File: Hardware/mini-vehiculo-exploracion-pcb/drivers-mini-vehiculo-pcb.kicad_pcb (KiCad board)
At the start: 2 copper layers, 26 parts, among them IC1 MAX8891EXK33_V+T, J1 Conn_01x08_Pin_drv, U1 DRV8873HPWPRQ1, U2 DRV8873HPWPRQ1, U3 TPS561208DDCR

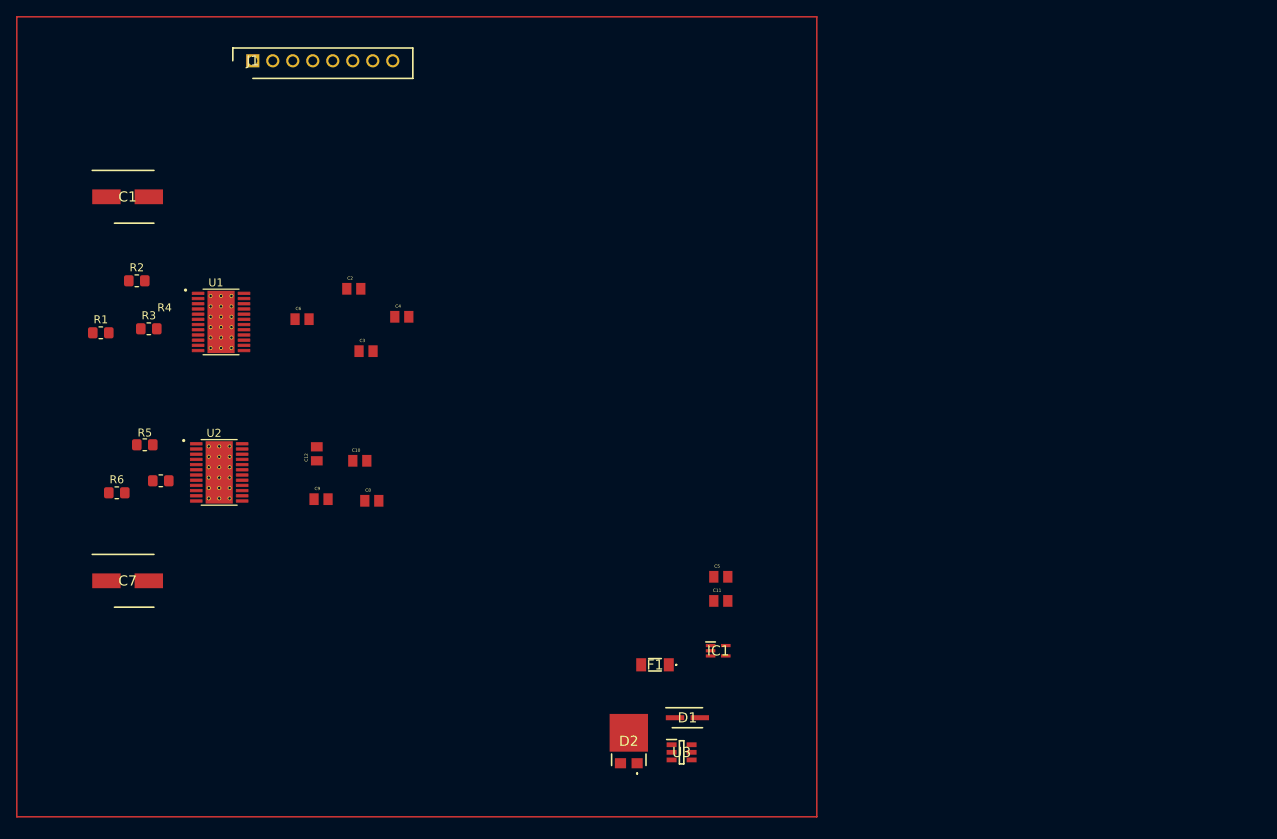
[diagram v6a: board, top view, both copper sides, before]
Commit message: adicion de bornera pcb drivers y organizacion de entrada
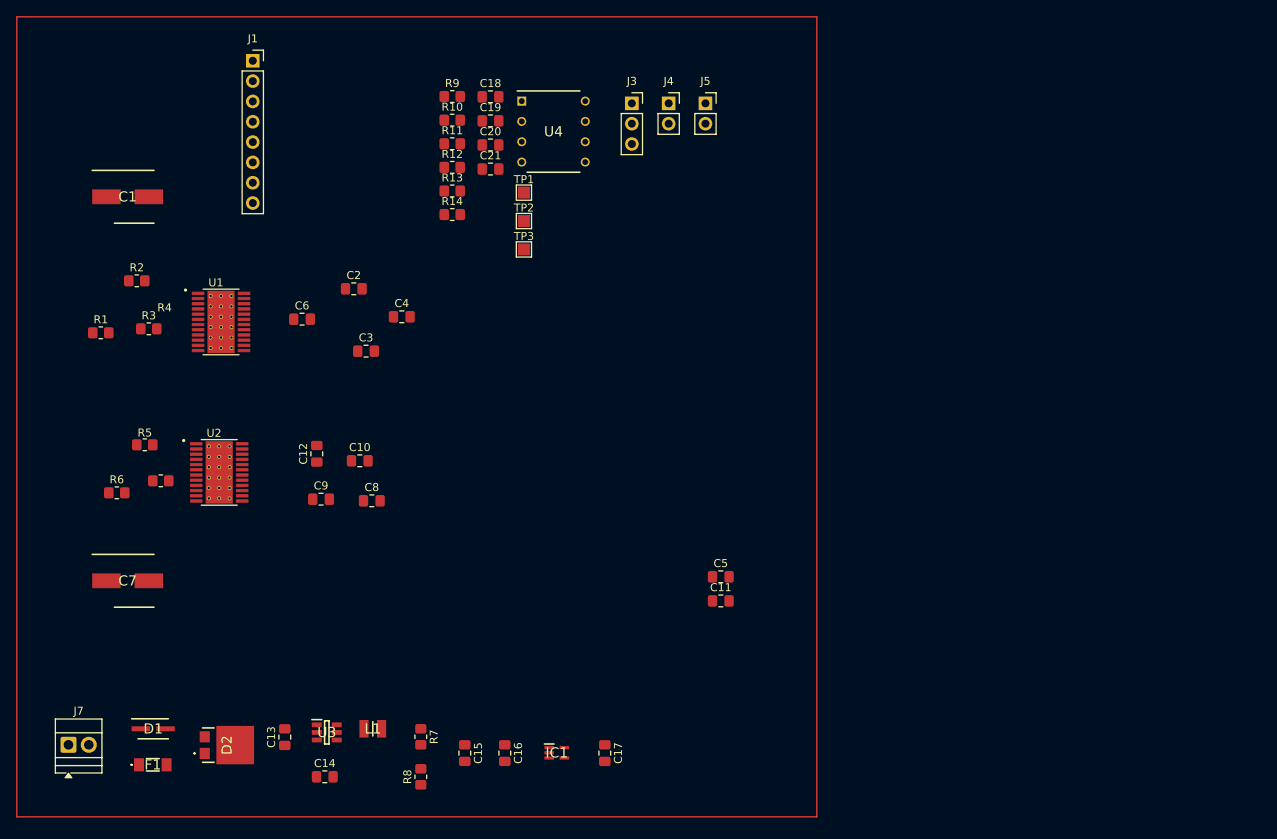
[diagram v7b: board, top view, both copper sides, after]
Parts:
- added C13: 10u, Capacitor_SMD:C_0805_2012Metric_Pad1.18x1.45mm_HandSolder, F.Cu at (58.0, 129.0)
- added C14: 100n, Capacitor_SMD:C_0805_2012Metric_Pad1.18x1.45mm_HandSolder, F.Cu at (63.0, 134.0)
- added C15: 47u, Capacitor_SMD:C_0805_2012Metric_Pad1.18x1.45mm_HandSolder, F.Cu at (80.5, 131.0)
- added C16: 1u, Capacitor_SMD:C_0805_2012Metric_Pad1.18x1.45mm_HandSolder, F.Cu at (85.5, 131.0)
- added C17: 1u, Capacitor_SMD:C_0805_2012Metric_Pad1.18x1.45mm_HandSolder, F.Cu at (98.0, 131.0)
- added C18: 10uF, Capacitor_SMD:C_0805_2012Metric_Pad1.18x1.45mm_HandSolder, F.Cu at (83.7, 49.0)
- added C19: 200nF, Capacitor_SMD:C_0805_2012Metric_Pad1.18x1.45mm_HandSolder, F.Cu at (83.7, 52.0)
- added C20: 10uF, Capacitor_SMD:C_0805_2012Metric_Pad1.18x1.45mm_HandSolder, F.Cu at (83.7, 55.0)
- added C21: 4.7u, Capacitor_SMD:C_0805_2012Metric_Pad1.18x1.45mm_HandSolder, F.Cu at (83.7, 58.0)
- added J3: Conn_01x03_Pin, Connector_PinSocket_2.54mm:PinSocket_1x03_P2.54mm_Vertical, F.Cu at (101.4, 49.8)
- added J4: Conn_01x02_Motor1, Connector_PinSocket_2.54mm:PinSocket_1x02_P2.54mm_Vertical, F.Cu at (106.0, 49.8)
- added J5: Conn_01x02_Motor2, Connector_PinSocket_2.54mm:PinSocket_1x02_P2.54mm_Vertical, F.Cu at (110.6, 49.8)
- added J7: Battery_Terminal_01x02, TerminalBlock:TerminalBlock_Xinya_XY308-2.54-2P_1x02_P2.54mm_Horizontal, F.Cu at (31.0, 130.0)
- added L1: MLP2520S4R7MT0S1, MLP2520S4R7MT0S1:INDC2520X100N, F.Cu at (69.0, 128.0)
- added R10: 10k, Resistor_SMD:R_0805_2012Metric_Pad1.20x1.40mm_HandSolder, F.Cu at (78.9, 51.9)
- added R11: 18k, Resistor_SMD:R_0805_2012Metric_Pad1.20x1.40mm_HandSolder, F.Cu at (78.9, 54.9)
- added R12: 20k, Resistor_SMD:R_0805_2012Metric_Pad1.20x1.40mm_HandSolder, F.Cu at (78.9, 57.8)
- added R13: 2k, Resistor_SMD:R_0805_2012Metric_Pad1.20x1.40mm_HandSolder, F.Cu at (78.9, 60.8)
- added R14: 2.7k, Resistor_SMD:R_0805_2012Metric_Pad1.20x1.40mm_HandSolder, F.Cu at (78.9, 63.7)
- added R7: 56,2k, Resistor_SMD:R_0805_2012Metric_Pad1.20x1.40mm_HandSolder, F.Cu at (75.0, 129.0)
- added R8: 10k, Resistor_SMD:R_0805_2012Metric_Pad1.20x1.40mm_HandSolder, F.Cu at (75.0, 134.0)
- added R9: 65k, Resistor_SMD:R_0805_2012Metric_Pad1.20x1.40mm_HandSolder, F.Cu at (78.9, 49.0)
- added TP1: Bat_div, TestPoint:TestPoint_Pad_1.5x1.5mm, F.Cu at (87.9, 61.0)
- added TP2: OP1_Out, TestPoint:TestPoint_Pad_1.5x1.5mm, F.Cu at (87.9, 64.5)
- added TP3: OP2_Out, TestPoint:TestPoint_Pad_1.5x1.5mm, F.Cu at (87.9, 68.1)
- added U4: LM358, LM358AN_NOPB:DIP794W53P254L959H508Q8N, F.Cu at (91.6, 53.4)
- C10, C11, C2, C3, C4, C5, C8, C9: footprint capacitores_driver:CAPC2012X88N -> Capacitor_SMD:C_0805_2012Metric_Pad1.18x1.45mm_HandSolder
- C12, C6: footprint capacitores_driver:CAPC2012X140N -> Capacitor_SMD:C_0805_2012Metric_Pad1.18x1.45mm_HandSolder
- J1: footprint JST_Connectors:JST_8PIN -> Connector_PinSocket_2.54mm:PinSocket_1x08_P2.54mm_Vertical
- U1, U2: footprint DRV8873HPWPRQ1:DRV8873HPWPRQ1 -> DRV8873HPWPRQ1:SOP65P640X120-25N
- moved D1 66.8 mm to (41.5, 128.0)
- moved F1 64.0 mm to (41.5, 132.5), turned to 0 degrees
- moved D2 50.2 mm to (50.8, 130.0), turned to -90 degrees
- moved U3 44.4 mm to (63.2, 128.4)
- moved IC1 23.9 mm to (92.0, 131.0)
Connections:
- C11 pad 1: DVDD -> DVDD_2
- C5 pad 1: DVDD -> DVDD_1
- IC1 pad 2: Net-(IC1-GND) -> GND
- U1 pad 1: DVDD -> DVDD_1
- U1 pad 11: DVDD -> DVDD_1
- U1 pad 25: Net-(U1-EXP-Pad25) -> unconnected-(U1-EXP-Pad25)_18
- U1 pad 3: DVDD -> DVDD_1
- U1 pad P1: Net-(U1-EXP-Pad25) -> unconnected-(U1-EXP-Pad25)_5
- U1 pad P10: Net-(U1-EXP-Pad25) -> unconnected-(U1-EXP-Pad25)_15
- U1 pad P11: Net-(U1-EXP-Pad25) -> unconnected-(U1-EXP-Pad25)_8
- U1 pad P12: Net-(U1-EXP-Pad25) -> unconnected-(U1-EXP-Pad25)_4
- U1 pad P13: Net-(U1-EXP-Pad25) -> unconnected-(U1-EXP-Pad25)_9
- U1 pad P14: Net-(U1-EXP-Pad25) -> unconnected-(U1-EXP-Pad25)_16
- U1 pad P15: Net-(U1-EXP-Pad25) -> unconnected-(U1-EXP-Pad25)_6
- U1 pad P16: Net-(U1-EXP-Pad25) -> unconnected-(U1-EXP-Pad25)_10
- U1 pad P17: Net-(U1-EXP-Pad25) -> unconnected-(U1-EXP-Pad25)
- U1 pad P18: Net-(U1-EXP-Pad25) -> unconnected-(U1-EXP-Pad25)_11
- U1 pad P2: Net-(U1-EXP-Pad25) -> unconnected-(U1-EXP-Pad25)_1
- U1 pad P3: Net-(U1-EXP-Pad25) -> unconnected-(U1-EXP-Pad25)_14
- U1 pad P4: Net-(U1-EXP-Pad25) -> unconnected-(U1-EXP-Pad25)_7
- U1 pad P5: Net-(U1-EXP-Pad25) -> unconnected-(U1-EXP-Pad25)_2
- U1 pad P6: Net-(U1-EXP-Pad25) -> unconnected-(U1-EXP-Pad25)_3
- U1 pad P7: Net-(U1-EXP-Pad25) -> unconnected-(U1-EXP-Pad25)_13
- U1 pad P8: Net-(U1-EXP-Pad25) -> unconnected-(U1-EXP-Pad25)_17
- U1 pad P9: Net-(U1-EXP-Pad25) -> unconnected-(U1-EXP-Pad25)_12
- U2 pad 1: DVDD -> DVDD_2
- U2 pad 11: DVDD -> DVDD_2
- U2 pad 25: Net-(U2-EXP-Pad25) -> unconnected-(U2-EXP-Pad25)_7
- U2 pad 3: DVDD -> DVDD_2
- U2 pad P1: Net-(U2-EXP-Pad25) -> unconnected-(U2-EXP-Pad25)_12
- U2 pad P10: Net-(U2-EXP-Pad25) -> unconnected-(U2-EXP-Pad25)_11
- U2 pad P11: Net-(U2-EXP-Pad25) -> unconnected-(U2-EXP-Pad25)_8
- U2 pad P12: Net-(U2-EXP-Pad25) -> unconnected-(U2-EXP-Pad25)_1
- U2 pad P13: Net-(U2-EXP-Pad25) -> unconnected-(U2-EXP-Pad25)_15
- U2 pad P14: Net-(U2-EXP-Pad25) -> unconnected-(U2-EXP-Pad25)_3
- U2 pad P15: Net-(U2-EXP-Pad25) -> unconnected-(U2-EXP-Pad25)_14
- U2 pad P16: Net-(U2-EXP-Pad25) -> unconnected-(U2-EXP-Pad25)_17
- U2 pad P17: Net-(U2-EXP-Pad25) -> unconnected-(U2-EXP-Pad25)_13
- U2 pad P18: Net-(U2-EXP-Pad25) -> unconnected-(U2-EXP-Pad25)_6
- U2 pad P2: Net-(U2-EXP-Pad25) -> unconnected-(U2-EXP-Pad25)_2
- U2 pad P3: Net-(U2-EXP-Pad25) -> unconnected-(U2-EXP-Pad25)
- U2 pad P4: Net-(U2-EXP-Pad25) -> unconnected-(U2-EXP-Pad25)_18
- U2 pad P5: Net-(U2-EXP-Pad25) -> unconnected-(U2-EXP-Pad25)_5
- U2 pad P6: Net-(U2-EXP-Pad25) -> unconnected-(U2-EXP-Pad25)_16
- U2 pad P7: Net-(U2-EXP-Pad25) -> unconnected-(U2-EXP-Pad25)_10
- U2 pad P8: Net-(U2-EXP-Pad25) -> unconnected-(U2-EXP-Pad25)_9
- U2 pad P9: Net-(U2-EXP-Pad25) -> unconnected-(U2-EXP-Pad25)_4
